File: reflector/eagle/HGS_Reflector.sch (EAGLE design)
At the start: 27 parts, among them J1 U.FL, U3 LP2985XX-N

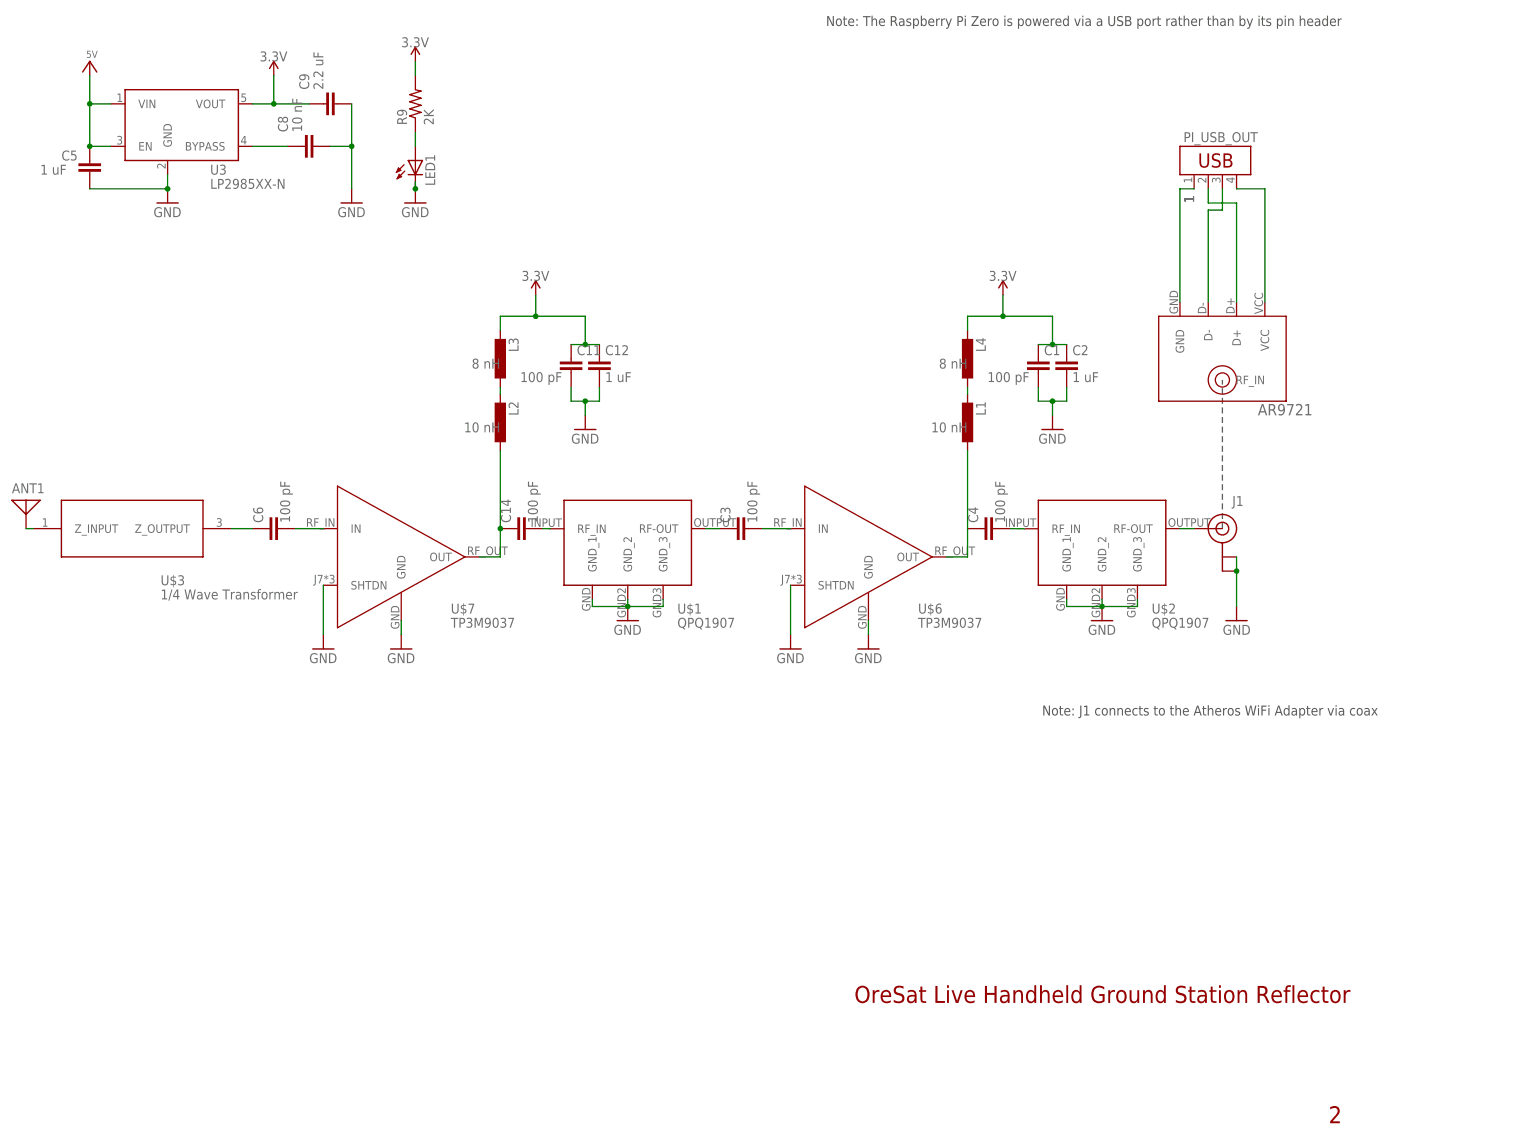
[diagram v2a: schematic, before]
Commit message: I completed the physical layout of the board for HGS. Currently, I just need to sort through some DRC errors that I don't know how to fix, and do a design review.
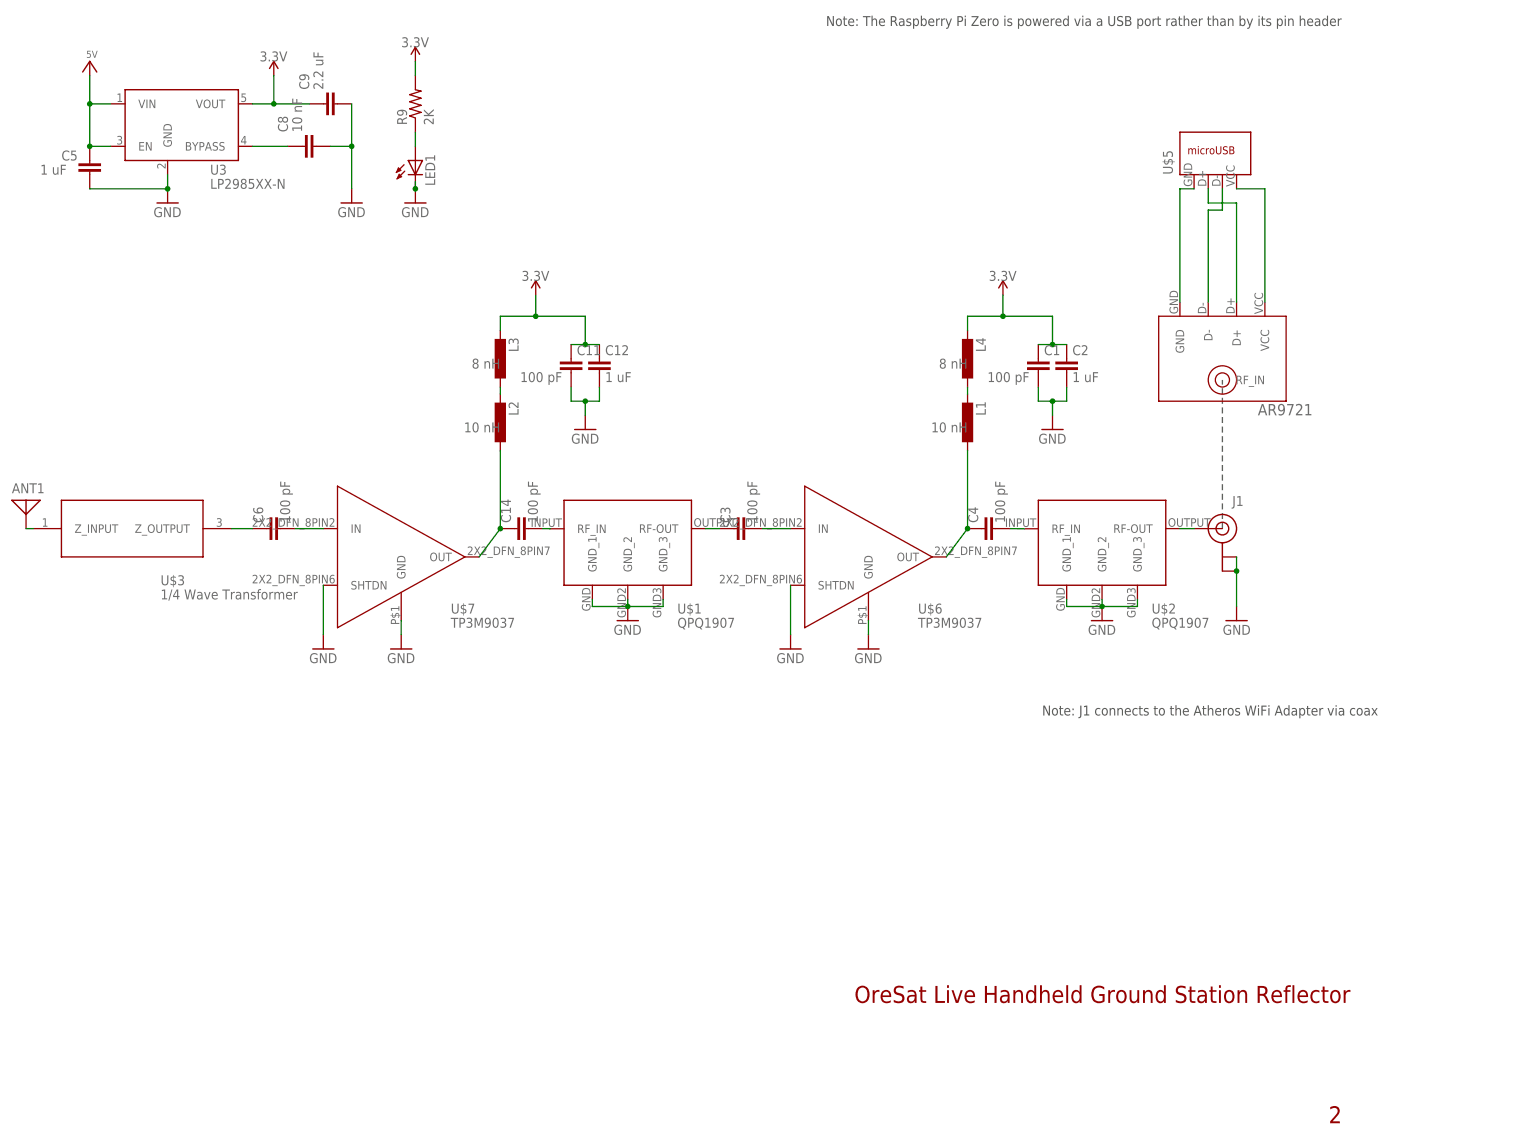
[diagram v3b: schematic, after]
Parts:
- removed PI_USB_OUT: (no value), con-amp:USB-787616
- added U$5: (no value), Rasp_Pi_0W:RASP_PI_0W
- U$6, U$7: device HGS_Data_Parts:LNA-TP3M9037 -> TP3M9037_LNA:LNA-TP3M9037
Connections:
- removed net 3.3V1: L4.2
- removed net N$2: C4.1, U$6.OUT
- net 1: no longer PI_USB_OUT.1
- net 3.3V: now also L4.2
- net N$13: now also C4.1, U$6.OUT
- net N$18: no longer PI_USB_OUT.2
- net N$19: no longer PI_USB_OUT.3
- net VCC: no longer PI_USB_OUT.4
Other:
- moved on the sheet: U$6, U$7
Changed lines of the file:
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@@
 </part>
 <part name="ANT1" library="discrete" library_urn="urn:adsk.eagle:library:211" deviceset="ANTENNA" device="" package3d_urn="urn:adsk.eagle:package:12928/1"/>
-<part name="PI_USB_OUT" library="con-amp" library_urn="urn:adsk.eagle:library:127" deviceset="USB-787616" device="" package3d_urn="urn:adsk.eagle:package:8081650/1"/>
 <part name="LED1" library="eagle-ltspice" library_urn="urn:adsk.eagle:library:217" deviceset="LED_E" device="" package3d_urn="urn:adsk.eagle:package:13319/2"/>
 <part name="GND11" library="supply1" library_urn="urn:adsk.eagle:library:371" deviceset="GND" device=""/>
@@
 <part name="3.3V4" library="oresat-supplies" deviceset="3.3V" device=""/>
 <part name="C14" library="oresat-rcl" deviceset="C-EU" device="0402-C-NOSILK" value="100 pF"/>
-<part name="U$7" library="HGS_Data_Parts" deviceset="LNA-TP3M9037" device=""/>
+<part name="U$7" library="TP3M9037_LNA" deviceset="LNA-TP3M9037" device=""/>
 <part name="GND3" library="supply1" library_urn="urn:adsk.eagle:library:371" deviceset="GND" device=""/>
 <part name="C3" library="oresat-rcl" deviceset="C-EU" device="0402-C-NOSILK" value="100 pF"/>
@@
 <attribute name="SPICEPREFIX" value="G"/>
 </part>
-<part name="U$6" library="HGS_Data_Parts" deviceset="LNA-TP3M9037" device=""/>
+<part name="U$6" library="TP3M9037_LNA" deviceset="LNA-TP3M9037" device=""/>
 <part name="GND4" library="supply1" library_urn="urn:adsk.eagle:library:371" deviceset="GND" device=""/>
 <part name="GND7" library="supply1" library_urn="urn:adsk.eagle:library:371" deviceset="GND" device=""/>
@@
 <part name="U$2" library="QPQ1907_BPF" deviceset="BPF" device=""/>
 <part name="U$4" library="AR9721" deviceset="AR9721" device=""/>
+<part name="U$5" library="Rasp_Pi_0W" deviceset="RASP_PI_0W" device=""/>
 </parts>
 <sheets>
@@
 <attribute name="VALUE" x="34.29" y="113.03" size="1.778" layer="96"/>
 </instance>
-<instance part="PI_USB_OUT" gate="G$1" x="246.38" y="179.07" smashed="yes" rot="R90">
-<attribute name="NAME" x="252.73" y="184.15" size="1.778" layer="95" rot="R180"/>
-<attribute name="VALUE" x="254" y="175.26" size="1.778" layer="96" rot="R90"/>
-</instance>
 <instance part="LED1" gate="G$1" x="101.6" y="179.07" smashed="yes">
 <attribute name="NAME" x="105.156" y="174.498" size="1.778" layer="95" rot="R90"/>
@@
 </instance>
 <instance part="U$4" gate="G$1" x="246.38" y="143.51" smashed="yes"/>
+<instance part="U$5" gate="G$1" x="246.38" y="179.07" smashed="yes" rot="R90">
+<attribute name="NAME" x="237.49" y="176.53" size="1.778" layer="95" rot="R90"/>
+<attribute name="VALUE" x="254" y="176.53" size="1.778" layer="96" rot="R90"/>
+</instance>
 </instances>
 <busses>
@@
 </segment>
 <segment>
-<pinref part="C9" gate="G$1" pin="1"/>
-<wire x1="82.55" y1="189.23" x2="76.2" y2="189.23" width="0.1524" layer="91"/>
-<pinref part="U3" gate="G$1" pin="VOUT"/>
-<wire x1="76.2" y1="189.23" x2="72.39" y2="189.23" width="0.1524" layer="91"/>
-<wire x1="76.2" y1="189.23" x2="76.2" y2="194.31" width="0.1524" layer="91"/>
-<junction x="76.2" y="189.23"/>
-<pinref part="3.3V4" gate="G$1" pin="3.3V"/>
-</segment>
-<segment>
-<wire x1="200.66" y1="151.13" x2="207.01" y2="151.13" width="0.1524" layer="91"/>
-<wire x1="207.01" y1="151.13" x2="215.9" y2="151.13" width="0.1524" layer="91"/>
 <pinref part="3.3V3" gate="G$1" pin="3.3V"/>
 <wire x1="207.01" y1="154.94" x2="207.01" y2="151.13" width="0.1524" layer="91"/>
-<junction x="207.01" y="151.13"/>
+<pinref part="L4" gate="G$1" pin="2"/>
+<wire x1="200.66" y1="148.59" x2="200.66" y2="151.13" width="0.1524" layer="91"/>
+<wire x1="200.66" y1="151.13" x2="207.01" y2="151.13" width="0.1524" layer="91"/>
 <pinref part="C2" gate="CE" pin="1"/>
 <pinref part="C1" gate="CE" pin="1"/>
 <wire x1="213.36" y1="146.05" x2="215.9" y2="146.05" width="0.1524" layer="91"/>
 <wire x1="215.9" y1="146.05" x2="218.44" y2="146.05" width="0.1524" layer="91"/>
-<wire x1="215.9" y1="151.13" x2="215.9" y2="146.05" width="0.1524" layer="91"/>
+<wire x1="215.9" y1="146.05" x2="215.9" y2="151.13" width="0.1524" layer="91"/>
+<wire x1="215.9" y1="151.13" x2="207.01" y2="151.13" width="0.1524" layer="91"/>
 <junction x="215.9" y="146.05"/>
+<junction x="207.01" y="151.13"/>
+</segment>
+<segment>
+<pinref part="3.3V4" gate="G$1" pin="3.3V"/>
+<wire x1="76.2" y1="194.31" x2="76.2" y2="189.23" width="0.1524" layer="91"/>
+<pinref part="C9" gate="G$1" pin="1"/>
+<wire x1="76.2" y1="189.23" x2="82.55" y2="189.23" width="0.1524" layer="91"/>
+<pinref part="U3" gate="G$1" pin="VOUT"/>
+<wire x1="76.2" y1="189.23" x2="72.39" y2="189.23" width="0.1524" layer="91"/>
+<junction x="76.2" y="189.23"/>
 </segment>
 </net>
@@
 <net name="1" class="0">
 <segment>
-<pinref part="PI_USB_OUT" gate="G$1" pin="1"/>
-<label x="241.3" y="171.45" size="1.778" layer="95" rot="R90"/>
-<label x="241.3" y="171.45" size="1.778" layer="95" rot="R90"/>
 <wire x1="238.76" y1="153.67" x2="238.76" y2="173.99" width="0.1524" layer="91"/>
 <wire x1="238.76" y1="173.99" x2="241.3" y2="173.99" width="0.1524" layer="91"/>
@@
 <segment>
 <pinref part="C14" gate="CE" pin="1"/>
+<wire x1="116.84" y1="113.03" x2="116.84" y2="127" width="0.1524" layer="91"/>
+<pinref part="L2" gate="G$1" pin="1"/>
 <pinref part="U$7" gate="G$1" pin="OUT"/>
-<wire x1="113.03" y1="107.95" x2="116.84" y2="107.95" width="0.1524" layer="91"/>
-<wire x1="116.84" y1="107.95" x2="116.84" y2="113.03" width="0.1524" layer="91"/>
-<wire x1="116.84" y1="113.03" x2="116.84" y2="127" width="0.1524" layer="91"/>
+<wire x1="113.03" y1="107.95" x2="116.84" y2="113.03" width="0.1524" layer="91"/>
 <junction x="116.84" y="113.03"/>
-<pinref part="L2" gate="G$1" pin="1"/>
 </segment>
 </net>
@@
 <net name="N$18" class="0">
 <segment>
-<pinref part="PI_USB_OUT" gate="G$1" pin="2"/>
 <wire x1="243.84" y1="173.99" x2="243.84" y2="171.45" width="0.1524" layer="91"/>
 <wire x1="243.84" y1="171.45" x2="248.92" y2="171.45" width="0.1524" layer="91"/>
@@
 <wire x1="243.84" y1="153.67" x2="243.84" y2="170.18" width="0.1524" layer="91"/>
 <wire x1="243.84" y1="170.18" x2="246.38" y2="170.18" width="0.1524" layer="91"/>
-<pinref part="PI_USB_OUT" gate="G$1" pin="3"/>
 <wire x1="246.38" y1="170.18" x2="246.38" y2="173.99" width="0.1524" layer="91"/>
 <pinref part="U$4" gate="G$1" pin="D-"/>
@@
 </segment>
 </net>
-<net name="N$2" class="0">
-<segment>
-<wire x1="200.66" y1="113.03" x2="200.66" y2="107.95" width="0.1524" layer="91"/>
-<wire x1="200.66" y1="107.95" x2="196.85" y2="107.95" width="0.1524" layer="91"/>
-<pinref part="C4" gate="CE" pin="1"/>
-<pinref part="U$6" gate="G$1" pin="OUT"/>
-</segment>
-</net>
 <net name="N$5" class="0">
 <segment>
@@
 </segment>
 </net>
-<net name="3.3V1" class="0">
-<segment>
-<pinref part="L4" gate="G$1" pin="2"/>
-<wire x1="200.66" y1="148.59" x2="200.66" y2="151.13" width="0.1524" layer="91"/>
-</segment>
-</net>
 <net name="N$13" class="0">
 <segment>
 <wire x1="200.66" y1="113.03" x2="200.66" y2="127" width="0.1524" layer="91"/>
 <pinref part="L1" gate="G$1" pin="1"/>
+<pinref part="U$6" gate="G$1" pin="OUT"/>
+<wire x1="196.85" y1="107.95" x2="200.66" y2="113.03" width="0.1524" layer="91"/>
+<pinref part="C4" gate="CE" pin="1"/>
+<junction x="200.66" y="113.03"/>
 </segment>
 </net>
@@
 <net name="VCC" class="0">
 <segment>
-<pinref part="PI_USB_OUT" gate="G$1" pin="4"/>
 <wire x1="248.92" y1="173.99" x2="254" y2="173.99" width="0.1524" layer="91"/>
 <wire x1="254" y1="173.99" x2="254" y2="153.67" width="0.1524" layer="91"/>

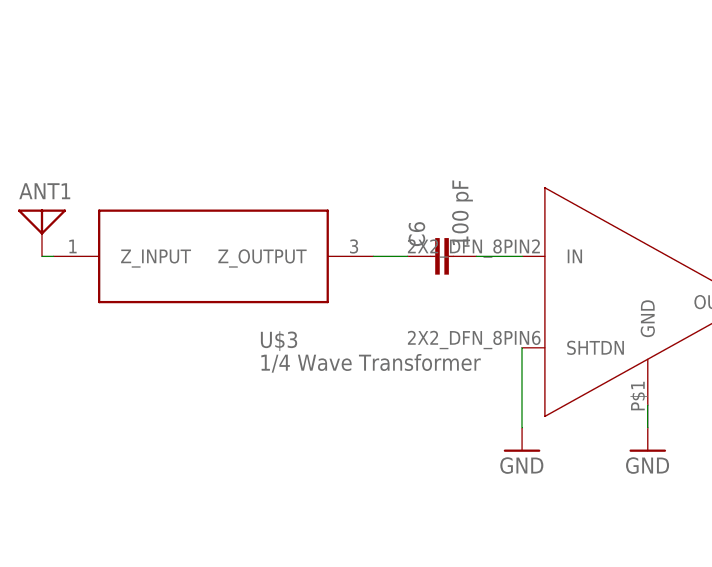
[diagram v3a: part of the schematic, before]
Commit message: I incorporated the 1/4 wave transformer part (TM-QWT-2.422GHz.lbr) into the HGS reflector board, but I have not yet consulted with the person who designed the part in order to situate it properly.
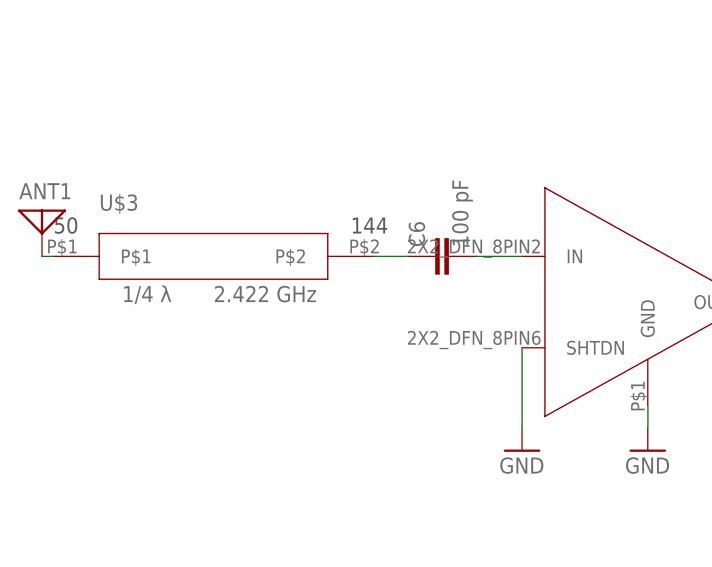
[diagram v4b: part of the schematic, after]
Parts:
- U$3: value 1/4_WAVE_TRF -> QWT2.422; device HGS_Data_Parts:1/4_WAVE_TRF -> TM-QWT-2.422GHz:QWT2.422
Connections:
- net N$12: now also U$3.P$1; no longer U$3.Z_INPUT
- net N$9: now also U$3.P$2; no longer U$3.Z_OUTPUT
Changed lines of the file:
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@@
 <part name="C12" library="oresat-rcl" deviceset="C-EU" device="0603-C-NOSILK" value="1 uF"/>
 <part name="3.3V1" library="oresat-supplies" deviceset="3.3V" device=""/>
-<part name="U$3" library="HGS_Data_Parts" deviceset="1/4_WAVE_TRF" device=""/>
 <part name="3.3V4" library="oresat-supplies" deviceset="3.3V" device=""/>
 <part name="C14" library="oresat-rcl" deviceset="C-EU" device="0402-C-NOSILK" value="100 pF"/>
@@
 <part name="U$4" library="AR9721" deviceset="AR9721" device=""/>
 <part name="U$5" library="Rasp_Pi_0W" deviceset="RASP_PI_0W" device=""/>
+<part name="U$3" library="TM-QWT-2.422GHz" deviceset="QWT2.422" device=""/>
 </parts>
 <sheets>
@@
 <attribute name="VALUE" x="120.65" y="157.48" size="1.778" layer="96"/>
 </instance>
-<instance part="U$3" gate="G$1" x="48.26" y="113.03" smashed="yes">
-<attribute name="NAME" x="55.88" y="102.87" size="1.778" layer="95"/>
-</instance>
 <instance part="3.3V4" gate="G$1" x="76.2" y="196.85" smashed="yes">
 <attribute name="VALUE" x="73.66" y="196.85" size="1.778" layer="96"/>
@@
 <attribute name="NAME" x="237.49" y="176.53" size="1.778" layer="95" rot="R90"/>
 <attribute name="VALUE" x="254" y="176.53" size="1.778" layer="96" rot="R90"/>
+</instance>
+<instance part="U$3" gate="G$1" x="50.8" y="113.03" smashed="yes">
+<attribute name="NAME" x="38.1" y="118.11" size="1.778" layer="95"/>
 </instance>
 </instances>
@@
 <pinref part="C6" gate="CE" pin="1"/>
 <wire x1="68.58" y1="113.03" x2="72.39" y2="113.03" width="0.1524" layer="91"/>
-<pinref part="U$3" gate="G$1" pin="Z_OUTPUT"/>
+<pinref part="U$3" gate="G$1" pin="P$2"/>
 </segment>
 </net>
@@
 <pinref part="ANT1" gate="A" pin="1"/>
 <wire x1="31.75" y1="113.03" x2="33.02" y2="113.03" width="0.1524" layer="91"/>
-<pinref part="U$3" gate="G$1" pin="Z_INPUT"/>
-</segment>
-</net>
+<pinref part="U$3" gate="G$1" pin="P$1"/>
+</segment>
+</net>
